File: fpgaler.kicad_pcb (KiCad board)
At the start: 4 copper layers, 188 x 165.2 mm, 319 parts, among them J1 USB_C_Receptacle_USB2.0, J2 BATT, J3 JTAG, J4 FTDI_RST, J5 VGA, J6 DB9 Expander, J7 DB9 Expander, Q1 BC817, SW1 RotaryEncoder_Switch, SW2 RotaryEncoder_Switch, SW3 K1, SW4 K2, SW5 PROGRAMN, SW6 K3, SW7 FPGA GSRN, SW8 K4, U1 TLV62569DRL, U10 XC6206PxxxMR, U11 IS62WV51216BLL-55TLI, U2 TLV62569DRL, U3 NCP115-2.5, U4 BQ24232, U5 93LC56BT-I/OT, U6 FT2232HL, U7 CAT24C128, U8 LFE5U-25F-8MG285C, U9 W25Q128JVP, X1 27MHz, Y1 7M-12.000MAAJ

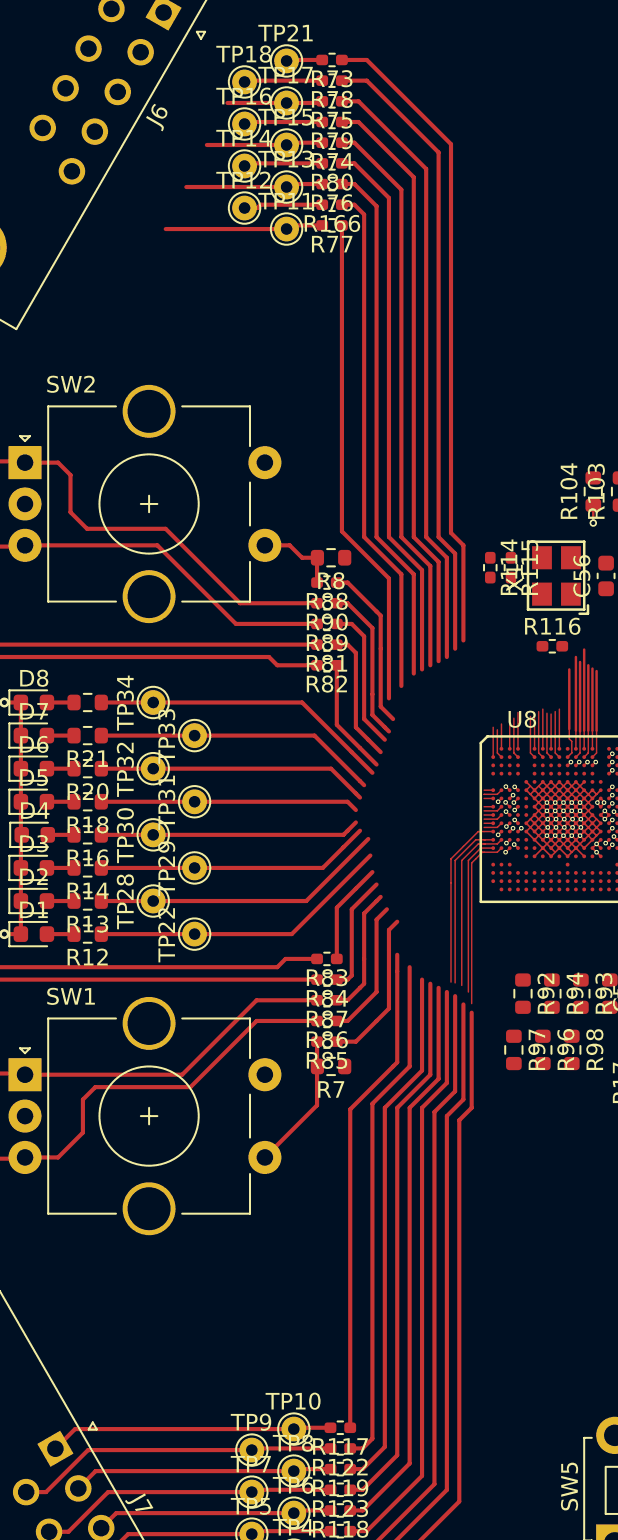
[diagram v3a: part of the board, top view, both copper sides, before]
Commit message: Route db9 connectors, rotary, btn and leds.
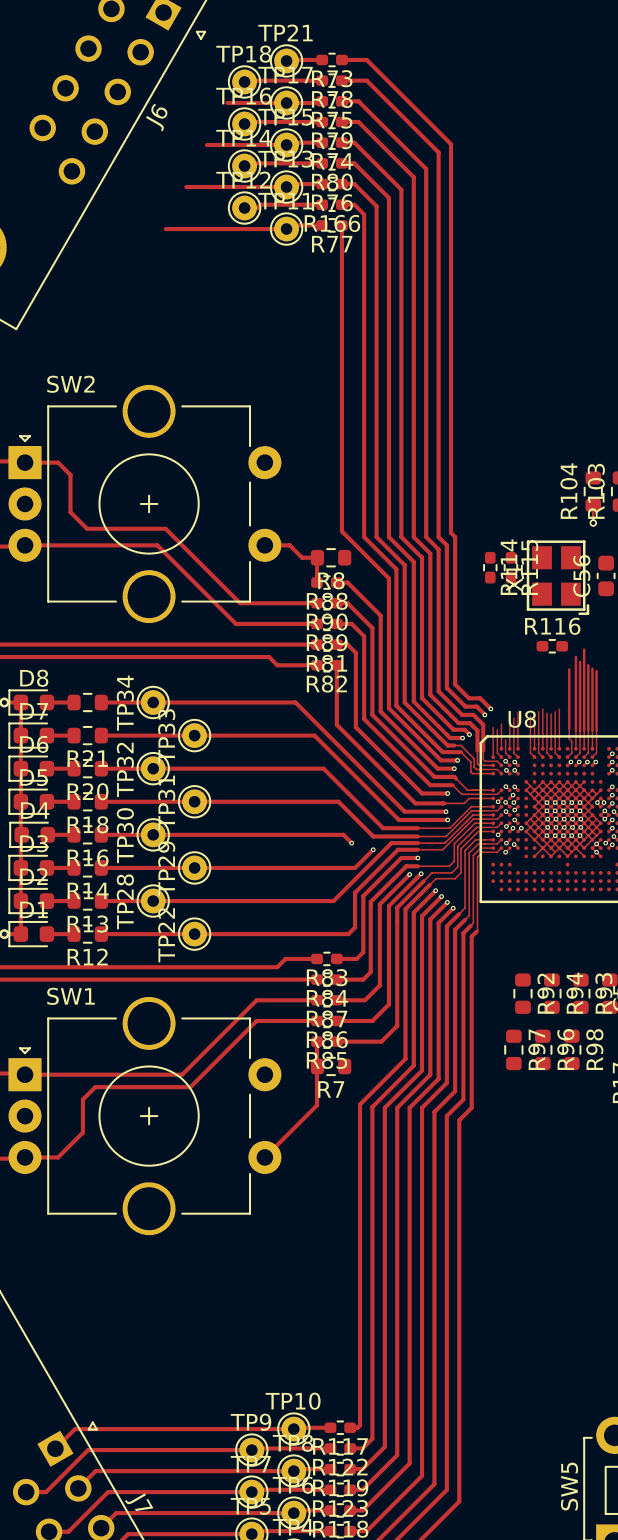
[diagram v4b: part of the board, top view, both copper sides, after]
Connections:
- R117 pad 1: Net-(U8D-PR26A/PCLKT3_1) -> Net-(U8D-PR44B)
- R118 pad 1: Net-(U8D-PR44B) -> Net-(U8D-PR38D)
- R119 pad 1: Net-(U8D-PR26C/PCLKT3_0) -> Net-(U8D-PR41A)
- R122 pad 1: Net-(U8D-PR29B) -> Net-(U8D-PR38B)
- R123 pad 1: Net-(U8D-PR29C/GR_PCLK3_1) -> Net-(U8D-PR38C)
- R166 pad 1: Net-(U8C-PR14A) -> Net-(U8C-PR23D/PCLKC2_0)
- R73 pad 1: Net-(U8C-PR2A) -> Net-(U8C-PR14B)
- R74 pad 1: Net-(U8C-PR2B/S0_IN) -> Net-(U8C-PR14A)
- R75 pad 1: Net-(U8C-PR5A) -> Net-(U8C-PR17B)
- R76 pad 1: Net-(U8C-PR5B) -> Net-(U8C-PR23A/PCLKT2_1)
- R77 pad 1: Net-(U8C-PR8A) -> Net-(U8D-PR26D/PCLKC3_0)
- R78 pad 1: Net-(U8C-PR8B) -> Net-(U8C-PR14D)
- R79 pad 1: Net-(U8C-PR11A) -> Net-(U8C-PR23C/PCLKT2_0)
- R80 pad 1: Net-(U8C-PR11B) -> Net-(U8C-PR17A)
- R81 pad 1: Net-(U8D-PR41A) -> Net-(U8D-PR29B)
- R82 pad 1: Net-(U8D-PR41B) -> Net-(U8D-PR32B)
- R83 pad 1: Net-(U8D-PR41C) -> Net-(U8D-PR38A)
- R86 pad 1: unconnected-(R86-Pad1) -> Net-(U8D-PR41B)
- R87 pad 1: unconnected-(R87-Pad1) -> Net-(U8D-PR41C)
- R88 pad 1: unconnected-(R88-Pad1) -> Net-(U8D-PR26C/PCLKT3_0)
- R89 pad 1: unconnected-(R89-Pad1) -> Net-(U8D-PR32A)
- R90 pad 1: unconnected-(R90-Pad1) -> Net-(U8D-PR35C)
- U8 pad A4: Net-(U8C-PR11B) -> unconnected-(U8C-PR11B-PadA4)
- U8 pad A6: Net-(U8C-PR11A) -> unconnected-(U8C-PR11A-PadA6)
- U8 pad A7: Net-(U8C-PR8B) -> unconnected-(U8C-PR8B-PadA7)
- U8 pad B6: Net-(U8C-PR8A) -> unconnected-(U8C-PR8A-PadB6)
- U8 pad B7: Net-(U8C-PR2B/S0_IN) -> unconnected-(U8C-PR2B/S0_IN-PadB7)
- U8 pad C1: unconnected-(U8C-PR23C/PCLKT2_0-PadC1) -> Net-(U8C-PR23C/PCLKT2_0)
- U8 pad C2: unconnected-(U8C-PR17B-PadC2) -> Net-(U8C-PR17B)
- U8 pad C3: unconnected-(U8C-PR14D-PadC3) -> Net-(U8C-PR14D)
- U8 pad C4: unconnected-(U8C-PR14B-PadC4) -> Net-(U8C-PR14B)
- U8 pad C6: Net-(U8C-PR5B) -> unconnected-(U8C-PR5B-PadC6)
- U8 pad C7: Net-(U8C-PR2A) -> unconnected-(U8C-PR2A-PadC7)
- U8 pad D1: unconnected-(U8C-PR23D/PCLKC2_0-PadD1) -> Net-(U8C-PR23D/PCLKC2_0)
- U8 pad D2: unconnected-(U8C-PR23A/PCLKT2_1-PadD2) -> Net-(U8C-PR23A/PCLKT2_1)
- U8 pad D3: unconnected-(U8C-PR17A-PadD3) -> Net-(U8C-PR17A)
- U8 pad D6: Net-(U8C-PR5A) -> unconnected-(U8C-PR5A-PadD6)
- U8 pad F1: /L5 -> Net-(U8D-PR35C)
- U8 pad F2: unconnected-(U8D-PR32A-PadF2) -> Net-(U8D-PR32A)
- U8 pad F3: unconnected-(U8D-PR26D/PCLKC3_0-PadF3) -> Net-(U8D-PR26D/PCLKC3_0)
- U8 pad G1: unconnected-(U8D-PR32B-PadG1) -> Net-(U8D-PR32B)
- U8 pad G4: unconnected-(U8D-PR26B/PCLKC3_1-PadG4) -> /L6
- U8 pad H1: /L4 -> /L5
- U8 pad H2: unconnected-(U8D-PR29D-PadH2) -> /L4
- U8 pad H3: /L0 -> /L7
- U8 pad H4: Net-(U8D-PR26A/PCLKT3_1) -> /L2
- U8 pad J1: /L6 -> /L1
- U8 pad J2: /L7 -> /L0
- U8 pad J3: Net-(U8D-PR29C/GR_PCLK3_1) -> /L3
- U8 pad K4: /L3 -> Net-(U8D-PR38A)
- U8 pad L4: /L2 -> Net-(U8D-PR38B)
- U8 pad N3: unconnected-(U8D-PR38D-PadN3) -> Net-(U8D-PR38D)
- U8 pad N4: /L1 -> Net-(U8D-PR38C)
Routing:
- net Net-(U8C-PR14B): track 0.00 -> 48.8 mm, vias 0 -> 2
- net Net-(U8C-PR14D): track 0.00 -> 47.3 mm, vias 0 -> 2
- net Net-(U8D-PR38D): track 0.00 -> 45.8 mm, vias 0 -> 2
- net Net-(U8C-PR17B): track 0.00 -> 45.6 mm
- net Net-(U8D-PR38C): track 0.00 -> 45.5 mm, vias 0 -> 2
- net Net-(U8D-PR38B): track 0.00 -> 44.5 mm, vias 0 -> 2
- net Net-(U8C-PR23C/PCLKT2_0): track 0.00 -> 44.2 mm
- net Net-(U8C-PR17A): track 0.00 -> 43.0 mm, vias 0 -> 2
- net Net-(U8C-PR23A/PCLKT2_1): track 0.00 -> 41.3 mm
- net Net-(U8C-PR8B): track 40.5 -> 0.00 mm
- net Net-(U8D-PR26D/PCLKC3_0): track 0.00 -> 40.3 mm, vias 0 -> 2
- net Net-(U8C-PR23D/PCLKC2_0): track 0.00 -> 40.0 mm
- net Net-(U8C-PR2A): track 39.0 -> 0.00 mm
- net Net-(U8C-PR11A): track 37.6 -> 0.00 mm
- net Net-(U8C-PR2B/S0_IN): track 37.1 -> 0.00 mm
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
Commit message: Continue routing
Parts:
- removed TP1: TestPoint, TestPoint:TestPoint_Pad_D1.0mm
- removed TP19, TP20, TP23, TP24: TestPoint, TestPoint:TestPoint_THTPad_D1.5mm_Drill0.7mm
- C26, C27, C29, C31, R48, R50: moved to F.Cu
- moved TP63 166.7 mm to (107.8, 29.8)
- moved TP26 162.0 mm to (129.3, 40.9)
- moved TP46 162.0 mm to (119.6, 34.6)
- moved TP25 162.0 mm to (130.0, 32.3)
- moved TP27 162.0 mm to (131.3, 37.6)
- moved TP40 162.0 mm to (126.2, 37.6)
- moved TP41 162.0 mm to (124.3, 32.1)
- moved TP42 162.0 mm to (123.3, 34.4)
- moved TP43 162.0 mm to (122.4, 40.1)
- moved TP44 162.0 mm to (123.7, 37.6)
- moved TP45 162.0 mm to (121.5, 31.5)
- moved TP62 160.2 mm to (111.8, 30.4)
- moved TP64 160.1 mm to (116.4, 31.2)
- moved TP58 159.1 mm to (115.7, 34.2)
- moved TP59 154.1 mm to (118.0, 37.1)
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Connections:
- C42 pad 1: +3.3V -> +1.1V
- C45 pad 1: +3.3V -> +1.1V
- C48 pad 1: +3.3V -> +2.5V
- C51 pad 1: +3.3V -> +2.5V
- R67 pad 1: unconnected-(R67-Pad1) -> Net-(U8C-PR5A)
- R68 pad 1: unconnected-(R68-Pad1) -> Net-(U8C-PR5B)
- R69 pad 1: unconnected-(R69-Pad1) -> Net-(U8C-PR2A)
- R70 pad 1: unconnected-(R70-Pad1) -> Net-(U8C-PR2B/S0_IN)
- U8 pad A7: unconnected-(U8C-PR8B-PadA7) -> /FPGA/scl
- U8 pad B6: unconnected-(U8C-PR8A-PadB6) -> /FPGA/sda
- U8 pad B7: unconnected-(U8C-PR2B/S0_IN-PadB7) -> Net-(U8C-PR2B/S0_IN)
- U8 pad C6: unconnected-(U8C-PR5B-PadC6) -> Net-(U8C-PR5B)
- U8 pad C7: unconnected-(U8C-PR2A-PadC7) -> Net-(U8C-PR2A)
- U8 pad D6: unconnected-(U8C-PR5A-PadD6) -> Net-(U8C-PR5A)
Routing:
- net SPI_CONFIG_MOSI: track 0.00 -> 28.7 mm, vias 0 -> 2
- net QSPI_D3: track 0.00 -> 27.2 mm, vias 0 -> 2
- net QSPI_D2: track 0.00 -> 22.0 mm, vias 0 -> 2
- net SPI_CONFIG_SS: track 0.00 -> 21.4 mm, vias 0 -> 2
- net SPI_CONFIG_MISO: track 0.00 -> 19.6 mm, vias 0 -> 2
- net /GSRN: track 0.00 -> 19.0 mm, vias 0 -> 2
- net /FT_TCK: track 2.10 -> 20.5 mm, vias 1 -> 2
- net /FT_TDI: track 2.10 -> 19.1 mm, vias 1 -> 2
- net /FT_TDO: track 2.10 -> 16.6 mm, vias 1 -> 2
- net /FT_TMS: track 2.10 -> 16.4 mm, vias 1 -> 2
- net /FPGA PWR/DONE: track 0.00 -> 11.8 mm
- net Net-(U8H-CFG_0): track 0.00 -> 11.5 mm
- net +3.3V: track 20.2 -> 8.64 mm, vias 11 -> 6
- net Net-(U6-BDBUS1): track 10.8 -> 0.00 mm
- net Net-(U8G-PB13A/SN/CSN): track 0.00 -> 10.7 mm, vias 0 -> 2
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
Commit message: continue routing
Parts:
- removed C12: 100nF, Capacitor_SMD:C_0603_1608Metric
- removed C20, C21: 4.7uF, Capacitor_SMD:C_0805_2012Metric
- removed D10: CHARGER, Diode_SMD:D_0603_1608Metric
- removed D9: PRESENT, Diode_SMD:D_0603_1608Metric
- removed J2: BATT, Connector_JST:JST_PH_S2B-PH-K_1x02_P2.00mm_Horizontal
- removed R25, R43: 10k, Resistor_SMD:R_0603_1608Metric
- removed R26, R41: 4.7k, Resistor_SMD:R_0603_1608Metric
- removed R35: 3.9k, Resistor_SMD:R_0603_1608Metric
- removed R36: 39k, Resistor_SMD:R_0603_1608Metric
- removed R37: 68k, Resistor_SMD:R_0603_1608Metric
- removed R38: 330k, Resistor_SMD:R_0603_1608Metric
- removed R39: 3.3k, Resistor_SMD:R_0603_1608Metric
- removed R40: 47k, Resistor_SMD:R_0603_1608Metric
- removed R42: 56k, Resistor_SMD:R_0603_1608Metric
- removed TP25, TP26, TP27, TP40, TP41, TP42, TP43, TP44, TP45, TP46, TP58, TP59, TP60, TP61, TP62, TP63, TP64, TP84, TP85: TestPoint, TestPoint:TestPoint_THTPad_D1.5mm_Drill0.7mm
- removed U4: BQ24232, Package_DFN_QFN:QFN-16-1EP_3x3mm_P0.5mm_EP1.75x1.75mm
- moved U3 45.6 mm to (150.3, 107.1), turned to -90 degrees
- moved U10 45.5 mm to (153.0, 106.8), turned to -90 degrees
- moved C11 45.4 mm to (153.1, 103.5), turned to 180 degrees
- moved C13 38.8 mm to (150.0, 104.0), turned to 90 degrees
- moved C14 37.8 mm to (157.2, 96.2), turned to 180 degrees
- moved R29 37.8 mm to (157.2, 94.5), turned to 0 degrees
- moved R30 35.7 mm to (160.5, 94.5), turned to 0 degrees
- moved R104 34.8 mm to (142.6, 30.4), turned to 0 degrees
- moved U1 32.7 mm to (157.2, 92.4), turned to 180 degrees
- moved R103 32.6 mm to (142.6, 32.0), turned to 0 degrees
- moved R27 30.6 mm to (160.5, 92.8), turned to 0 degrees
- moved L1 30.1 mm to (156.8, 90.2), turned to 180 degrees
- moved C16 29.0 mm to (152.5, 93.0)
- moved C18 29.0 mm to (152.5, 90.5)
- moved R113 28.8 mm to (142.6, 34.8), turned to 0 degrees
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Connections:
- C10 pad 2: VSYS -> +5V
- C9 pad 2: VSYS -> +5V
- R27 pad 2: VSYS -> +5V
- R28 pad 2: VSYS -> +5V
- R33 pad 1: Net-(R33-Pad1) -> Net-(U2-FB)
- R34 pad 1: Net-(R33-Pad1) -> Net-(U2-FB)
- U1 pad 3: VSYS -> +5V
- U2 pad 3: VSYS -> +5V
- U8 pad A8: Net-(U8B-PT35B/PCLKC1_0) -> unconnected-(U8B-PT35B/PCLKC1_0-PadA8)
- U8 pad B8: Net-(U8B-PT67A) -> unconnected-(U8B-PT67A-PadB8)
- U8 pad C8: Net-(U8B-PT67B) -> unconnected-(U8B-PT67B-PadC8)
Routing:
- net GND: track 116.3 -> 710.0 mm, vias 39 -> 95
- net +3.3V: track 8.64 -> 97.3 mm, vias 6 -> 34
- net /FT_TMS: track 16.4 -> 76.1 mm
- net /FT_TCK: track 20.5 -> 78.1 mm
- net /PROGRAMN: track 7.36 -> 63.7 mm, vias 2 -> 3
- net Net-(U8C-PR5B): track 0.00 -> 54.5 mm, vias 0 -> 1
- net /GSRN: track 19.0 -> 69.1 mm, vias 2 -> 4
- net Net-(U8C-PR2B/S0_IN): track 0.00 -> 48.6 mm, vias 0 -> 1
- net Net-(U8C-PR5A): track 0.00 -> 45.5 mm, vias 0 -> 1
- net Net-(U8C-PR2A): track 0.00 -> 45.1 mm, vias 0 -> 1
- net /FT_TDI: track 19.1 -> 62.8 mm
- net /FT_TDO: track 16.6 -> 59.6 mm
- net EN: track 0.00 -> 35.5 mm, vias 0 -> 5
- net VCC1_8FT: track 0.00 -> 21.8 mm, vias 0 -> 4
- net /V_USB: track 0.00 -> 19.2 mm, vias 0 -> 5
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
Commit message: Start routing pwr
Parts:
- added FB4: 15Ω@100MHz, Inductor_SMD:L_0603_1608Metric_Pad1.05x0.95mm_HandSolder, F.Cu at (152.5, 102.2)
- added FB5: 15Ω@100MHz, Inductor_SMD:L_0603_1608Metric_Pad1.05x0.95mm_HandSolder, F.Cu at (147.0, 104.8)
- added FB6: 15Ω@100MHz, Inductor_SMD:L_0603_1608Metric_Pad1.05x0.95mm_HandSolder, F.Cu at (153.0, 95.2)
- added TP1: TestPoint, TestPoint:TestPoint_THTPad_D1.5mm_Drill0.7mm, F.Cu at (109.3, 25.4)
- added TP19: TestPoint, TestPoint:TestPoint_THTPad_D1.5mm_Drill0.7mm, F.Cu at (109.2, 30.5)
- added TP20: TestPoint, TestPoint:TestPoint_THTPad_D1.5mm_Drill0.7mm, F.Cu at (109.2, 134.6)
- added TP23: TestPoint, TestPoint:TestPoint_THTPad_D1.5mm_Drill0.7mm, F.Cu at (109.2, 129.5)
- added TP24: TestPoint, TestPoint:TestPoint_THTPad_D1.5mm_Drill0.7mm, F.Cu at (109.2, 27.9)
- added TP25: TestPoint, TestPoint:TestPoint_THTPad_D1.5mm_Drill0.7mm, F.Cu at (109.2, 132.1)
- moved C48 3.50 mm to (122.2, 86.2)
- moved C51 3.50 mm to (120.5, 86.2)
- moved C42 3.50 mm to (118.8, 86.2)
- moved C45 3.50 mm to (117.0, 86.2)
- moved C13 1.31 mm to (148.9, 104.8)
- moved U10 1.31 mm to (151.9, 107.5)
- moved U3 1.31 mm to (149.2, 107.8)
- moved C11 1.31 mm to (152.0, 104.2)
- moved R10 1.03 mm to (141.5, 106.2)
- moved R9 1.03 mm to (141.5, 105.2)
- moved C17 1.00 mm to (152.5, 97.5)
- moved C19 1.00 mm to (152.5, 100.0)
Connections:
- net /FTDI/DM renamed /FTDI/D_N
- net /FTDI/DP renamed /FTDI/D_P
- net /_USB_D_N renamed /USB_N
- net /_USB_D_P renamed /USB_P
- C13 pad 1: +2.5V -> Net-(U10-VO)
- C14 pad 2: +1.1V -> Net-(C14-Pad2)
- C15 pad 2: +3.3V -> Net-(C15-Pad2)
- C16 pad 2: +1.1V -> Net-(C14-Pad2)
- C17 pad 2: +3.3V -> Net-(C15-Pad2)
- C18 pad 2: +1.1V -> Net-(C14-Pad2)
- C19 pad 2: +3.3V -> Net-(C15-Pad2)
- L1 pad 2: +1.1V -> Net-(C14-Pad2)
- L2 pad 2: +3.3V -> Net-(C15-Pad2)
- R29 pad 1: +1.1V -> Net-(C14-Pad2)
- R31 pad 2: +3.3V -> Net-(C15-Pad2)
- R33 pad 2: +3.3V -> Net-(C15-Pad2)
- U10 pad 2: +2.5V -> Net-(U10-VO)
- U3 pad 1: +2.5V -> Net-(U10-VO)
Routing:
- net +3.3V: track 97.3 -> 507.7 mm, vias 34 -> 60
- net GND: track 710.0 -> 1001.6 mm, vias 95 -> 118
- net +2.5V: track 6.12 -> 60.4 mm, vias 1 -> 6
- net Net-(C15-Pad2): track 0.00 -> 30.8 mm, vias 0 -> 9
- net VCC1_8FT: track 21.8 -> 48.7 mm, vias 4 -> 5
- net /FPGA/scl: track 0.00 -> 24.6 mm, vias 0 -> 2
- net /FPGA/sda: track 0.00 -> 22.5 mm, vias 0 -> 2
- net /USB_P: track 0.00 -> 21.3 mm
- net /USB_N: track 0.00 -> 19.6 mm
- net +1.1V: track 13.0 -> 28.7 mm, vias 4 -> 12
- net /P1_DB9: track 4.78 -> 19.0 mm
- net /P1_DB8: track 4.76 -> 17.5 mm
- net Net-(C14-Pad2): track 0.00 -> 11.8 mm
- net /P1_DB7: track 4.74 -> 16.1 mm
- net /P1_DB6: track 4.73 -> 14.6 mm
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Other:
- board text added: "JLC04161H-7628(Standard/Finished thickness1.59mm±10%)"

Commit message: continue planes routing
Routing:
- net GND: track 1001.6 -> 1108.4 mm, vias 118 -> 119
- net +3.3V: track 507.7 -> 547.3 mm
- net /FPGA/VGA_VSYNC: track 15.2 -> 54.8 mm
- net /FPGA/VGA_HSYNC: track 15.7 -> 53.3 mm
- net /FPGA/VGA_R2: track 14.3 -> 50.1 mm, vias 1 -> 2
- net /FPGA/VGA_R1: track 14.4 -> 47.5 mm, vias 1 -> 0
- net /FPGA/VGA_R0: track 14.7 -> 46.8 mm
- net /FPGA/VGA_G2: track 15.3 -> 44.8 mm
- net /FPGA/VGA_G1: track 16.0 -> 43.5 mm
- net /FPGA/VGA_G0: track 15.1 -> 42.4 mm
- net /VSYNC: track 0.00 -> 26.2 mm
- net /FPGA/VGA_B2: track 12.5 -> 38.6 mm
- net /FPGA/VGA_B1: track 12.9 -> 36.8 mm
- net /HSYNC: track 0.00 -> 22.3 mm
- net /FPGA/VGA_B0: track 14.6 -> 36.5 mm
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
